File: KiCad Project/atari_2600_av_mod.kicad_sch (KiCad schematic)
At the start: 20 parts, among them J1 INPUT, J2 OUTPUT, J3 Conn_01x01_Pin, J4 Conn_01x01_Pin, J5 Conn_01x01_Pin, J6 Conn_01x01_Pin, Q1 2SC1815, U1 4050

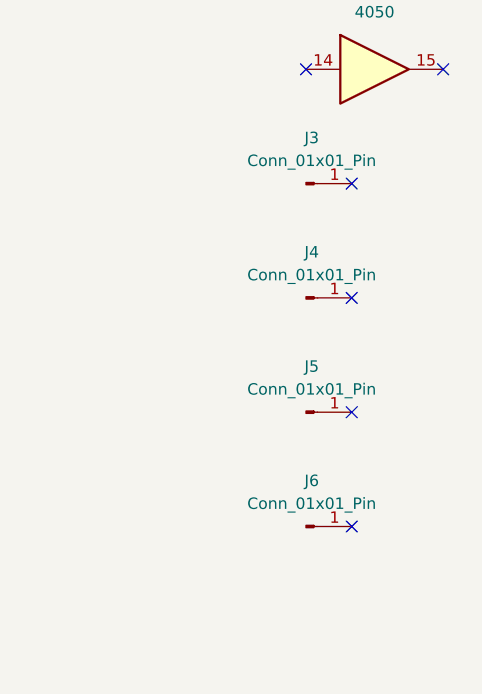
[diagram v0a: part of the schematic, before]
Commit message: v1.1.0
- Updated 2SC1815 footprint.
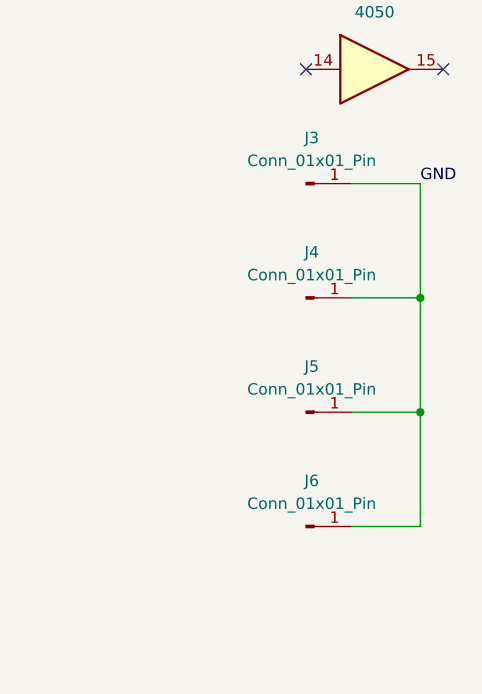
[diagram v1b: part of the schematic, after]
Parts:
- Q1: footprint Package_TO_SOT_THT:TO-92_Inline -> Package_TO_SOT_THT:TO-92_HandSolder
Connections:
- net GND: now also J3.1 (Pin_1), J4.1 (Pin_1), J5.1 (Pin_1), J6.1 (Pin_1)
- no-connect marks 6 -> 2
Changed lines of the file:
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@@
   (title_block
     (title "Atari 2600 AV MOD (PAL Version)")
-    (date "2023-08-20")
-    (rev "4")
+    (date "2023-08-28")
+    (rev "5")
     (comment 1 "nightfoxandco.com")
     (comment 2 "NightFox & Co")
@@
   (junction (at 146.05 102.87) (diameter 0) (color 0 0 0 0)
   )
+  (junction (at 368.3 63.5) (diameter 0) (color 0 0 0 0)
+  )
   (junction (at 146.05 77.47) (diameter 0) (color 0 0 0 0)
   )
@@
   (junction (at 222.25 107.95) (diameter 0) (color 0 0 0 0)
   )
+  (junction (at 368.3 50.8) (diameter 0) (color 0 0 0 0)
+  )
   (junction (at 146.05 24.13) (diameter 0) (color 0 0 0 0)
   )
   (junction (at 107.95 64.77) (diameter 0) (color 0 0 0 0)
   )
-  (no_connect (at 360.68 63.5))
   (no_connect (at 370.84 25.4))
-  (no_connect (at 360.68 76.2))
-  (no_connect (at 360.68 38.1))
-  (no_connect (at 360.68 50.8))
   (no_connect (at 355.6 25.4))
   (wire (pts (xy 222.25 107.95) (xy 247.65 107.95))
@@
     (stroke (width 0) (type default))
   )
+  (wire (pts (xy 368.3 50.8) (xy 360.68 50.8))
+    (stroke (width 0) (type default))
+  )
   (wire (pts (xy 69.85 128.27) (xy 69.85 77.47))
     (stroke (width 0) (type default))
@@
     (stroke (width 0) (type default))
   )
+  (wire (pts (xy 368.3 63.5) (xy 360.68 63.5))
+    (stroke (width 0) (type default))
+  )
   (wire (pts (xy 76.2 74.93) (xy 44.45 74.93))
     (stroke (width 0) (type default))
@@
     (stroke (width 0) (type default))
   )
+  (wire (pts (xy 368.3 50.8) (xy 368.3 63.5))
+    (stroke (width 0) (type default))
+  )
   (wire (pts (xy 129.54 115.57) (xy 146.05 115.57))
     (stroke (width 0) (type default))
@@
     (stroke (width 0) (type default))
   )
+  (wire (pts (xy 368.3 38.1) (xy 368.3 50.8))
+    (stroke (width 0) (type default))
+  )
   (wire (pts (xy 146.05 115.57) (xy 146.05 128.27))
     (stroke (width 0) (type default))
@@
     (stroke (width 0) (type default))
   )
+  (wire (pts (xy 360.68 38.1) (xy 368.3 38.1))
+    (stroke (width 0) (type default))
+  )
   (wire (pts (xy 146.05 176.53) (xy 146.05 163.83))
     (stroke (width 0) (type default))
@@
     (stroke (width 0) (type default))
   )
+  (wire (pts (xy 368.3 63.5) (xy 368.3 76.2))
+    (stroke (width 0) (type default))
+  )
   (wire (pts (xy 82.55 72.39) (xy 44.45 72.39))
     (stroke (width 0) (type default))
@@
   )
   (wire (pts (xy 69.85 24.13) (xy 69.85 40.64))
+    (stroke (width 0) (type default))
+  )
+  (wire (pts (xy 368.3 76.2) (xy 360.68 76.2))
     (stroke (width 0) (type default))
   )
@@
   (text "LUMA 2 (TIA PIN 06)" (at 35.56 71.12 0)
     (effects (font (face "Consolas") (size 1.27 1.27)) (justify right bottom))
+  )
+  (label "GND" (at 368.3 38.1 0) (fields_autoplaced)
+    (effects (font (size 1.27 1.27)) (justify left bottom))
   )
   (label "GND" (at 107.95 64.77 0) (fields_autoplaced)
@@
       (effects (font (size 1.27 1.27)) (justify left))
     )
-    (property "Footprint" "Package_TO_SOT_THT:TO-92_Inline" (at 199.39 89.535 0)
+    (property "Footprint" "Package_TO_SOT_THT:TO-92_HandSolder" (at 199.39 89.535 0)
       (effects (font (size 1.27 1.27) italic) (justify left) hide)
     )
